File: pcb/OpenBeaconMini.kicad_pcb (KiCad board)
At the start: 2 copper layers, 100 x 80 mm, 122 parts, among them J1 Bias V, J10 BNC, J2 PAI+, J3 PAI-, J4 Digital IO, J5 SMA, J6 SMA, J7 I2C Bus, J8 ADC Inputs, J9 GND, M1 LPFModule, Q1 2N7002, Q2 MMBT4403, Q3 RD00HVS1, Q4 2N7002, Q5 2N7002, U1 TLV61046A, U2 ASTX-H11-25.000MHZ-T, U3 SN74LVC1G17, U4 SI5351A, U5 MCP4725A1T-E/CH, U6 128x32OLED, U7 Empyrean

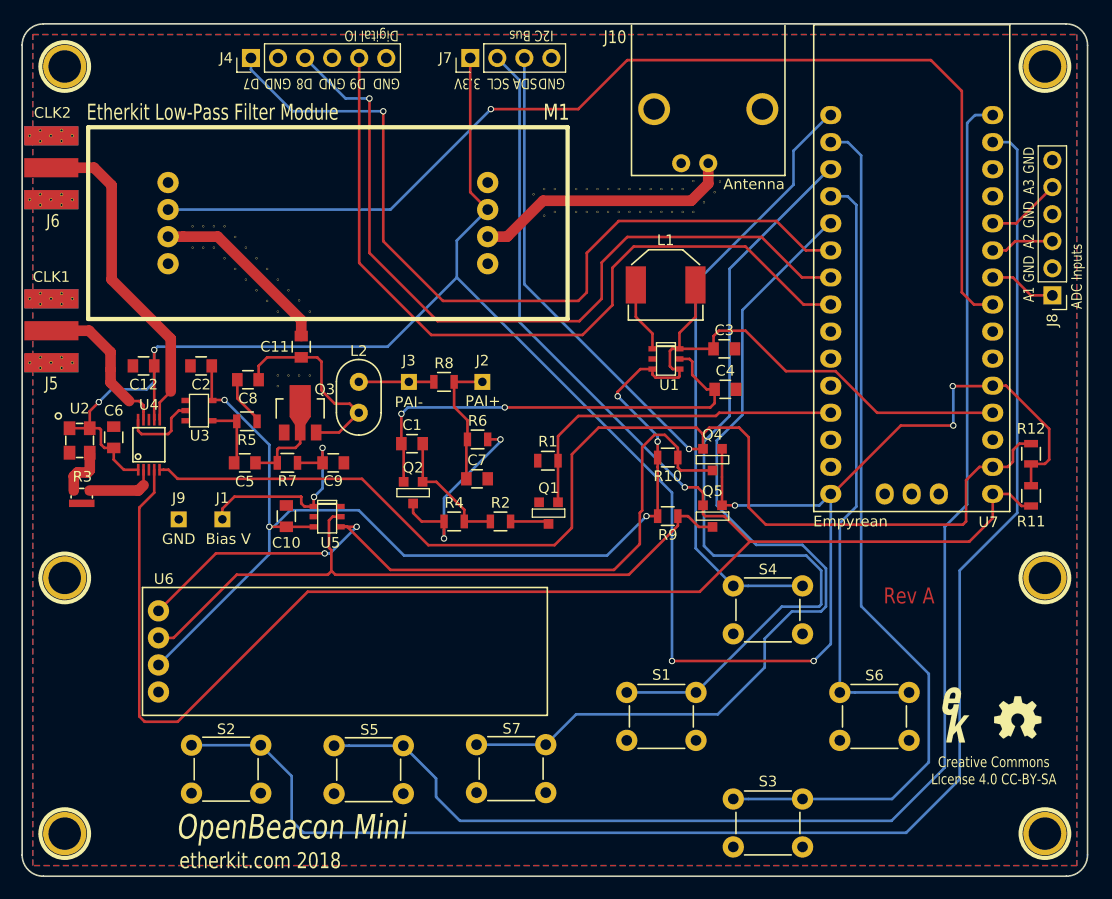
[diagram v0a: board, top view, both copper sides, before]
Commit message: Initial sl support for FT8
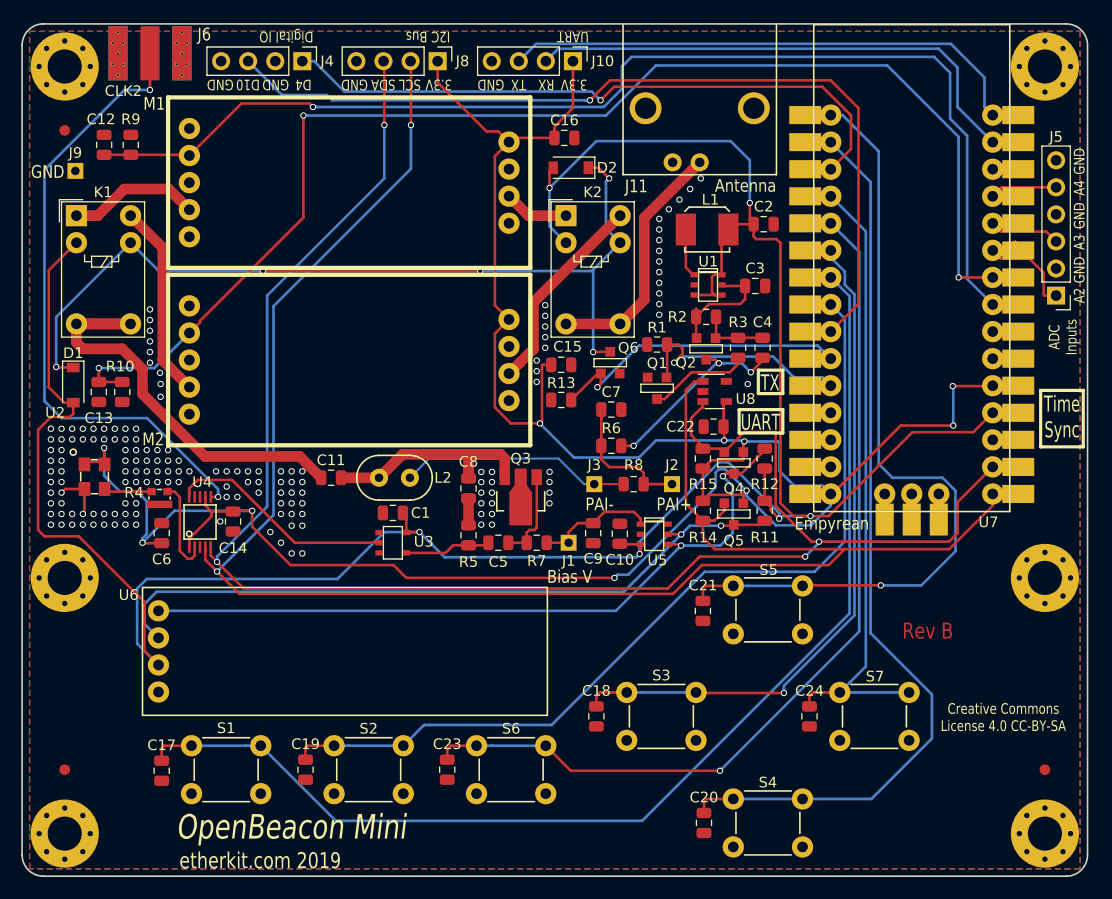
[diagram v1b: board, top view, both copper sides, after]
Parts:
- removed 1PIN (x6): P***, EtherkitKicadLibrary:MOUNTINGHOLE-4MM
- removed G***: LOGO, EtherkitKicadLibrary:OSHWLogo4mm
- removed J7: I2C Bus, Pin_Headers:Pin_Header_Straight_1x04_Pitch2.54mm
- removed Ref**: Val**, EtherkitKicadLibrary:EtherkitLogoSmall
- removed VIA (x58): VAL**, EtherkitKicadLibrary:VIA
- added C13: 100n, Capacitor_SMD:C_0805_2012Metric, F.Cu at (107.2, 84.5)
- added C14: 100n, Capacitor_SMD:C_0805_2012Metric, F.Cu at (119.8, 96.7)
- added C15: 4.7u, Capacitor_SMD:C_0805_2012Metric, F.Cu at (150.6, 82.0)
- added C16: 4.7u, Capacitor_SMD:C_0805_2012Metric, F.Cu at (150.9, 60.7)
- added C17: 100n, Capacitor_SMD:C_0805_2012Metric, F.Cu at (113.1, 120.1)
- added C18: 100n, Capacitor_SMD:C_0805_2012Metric, F.Cu at (153.9, 115.0)
- added C19: 100n, Capacitor_SMD:C_0805_2012Metric, F.Cu at (126.6, 120.0)
- added C20: 100n, Capacitor_SMD:C_0805_2012Metric, F.Cu at (164.0, 125.0)
- added C21: 100n, Capacitor_SMD:C_0805_2012Metric, F.Cu at (163.9, 105.1)
- added C22: 100n, Capacitor_SMD:C_0805_2012Metric, F.Cu at (164.9, 87.8)
- added C23: 100n, Capacitor_SMD:C_0805_2012Metric, F.Cu at (139.9, 120.0)
- added C24: 100n, Capacitor_SMD:C_0805_2012Metric, F.Cu at (173.9, 115.0)
- added D1: 1N4148W, Diode_SMD:D_SOD-123, F.Cu at (104.8, 83.9)
- added D2: 1N4148W, Diode_SMD:D_SOD-123, F.Cu at (151.5, 63.5)
- added J11: BNC, EtherkitKicadLibrary:BNC-AMPHENOL-31-5431-10RFX, F.Cu at (163.6, 50.0)
- added K1: G5V-1-DC5, Relay_THT:Relay_SPDT_Omron_G5V-1, F.Cu at (105.1, 68.0)
- added K2: G5V-1-DC5, Relay_THT:Relay_SPDT_Omron_G5V-1, F.Cu at (151.1, 68.0)
- added M2: LPF 2, EtherkitKicadLibrary:LPFModule, F.Cu at (130.7, 81.5)
- added Q6: 2N7002, EtherkitKicadLibrary:SOT23-2N7002, F.Cu at (155.2, 81.8)
- added R13: 22k, Resistor_SMD:R_0805_2012Metric, F.Cu at (150.6, 85.3)
- added R14: 3.3k, Resistor_SMD:R_0805_2012Metric, F.Cu at (163.9, 95.7)
- added R15: 3.3k, Resistor_SMD:R_0805_2012Metric, F.Cu at (163.9, 90.8)
- added REF**: Fiducial_1mm_Dia_2.54mm_Outer_CopperTop, Fiducial:Fiducial_1mm_Dia_2.54mm_Outer_CopperTop, F.Cu at (104.0, 60.0)
- added REF**: Fiducial_1mm_Dia_2.54mm_Outer_CopperTop, Fiducial:Fiducial_1mm_Dia_2.54mm_Outer_CopperTop, F.Cu at (196.0, 120.0)
- added REF**: MountingHole_3.2mm_M3_Pad_Via, MountingHole:MountingHole_3.2mm_M3_Pad_Via, F.Cu at (196.0, 102.0)
- added REF**: MountingHole_3.2mm_M3_Pad_Via, MountingHole:MountingHole_3.2mm_M3_Pad_Via, F.Cu at (104.0, 102.0)
- added REF**: MountingHole_3.2mm_M3_Pad_Via, MountingHole:MountingHole_3.2mm_M3_Pad_Via, F.Cu at (104.0, 54.0)
- added REF**: MountingHole_3.2mm_M3_Pad_Via, MountingHole:MountingHole_3.2mm_M3_Pad_Via, F.Cu at (196.0, 54.0)
- added REF**: MountingHole_3.2mm_M3_Pad_Via, MountingHole:MountingHole_3.2mm_M3_Pad_Via, F.Cu at (196.0, 126.0)
- added REF**: MountingHole_3.2mm_M3_Pad_Via, MountingHole:MountingHole_3.2mm_M3_Pad_Via, F.Cu at (104.0, 126.0)
- added REF**: Fiducial_1mm_Dia_2.54mm_Outer_CopperTop, Fiducial:Fiducial_1mm_Dia_2.54mm_Outer_CopperTop, F.Cu at (104.0, 120.0)
- added U8: 24AA64T, Package_TO_SOT_SMD:SOT-23-5, F.Cu at (165.0, 84.5)
- C1: value 10n -> 100n; footprint EtherkitKicadLibrary:C_0805 -> Capacitor_SMD:C_0805_2012Metric
- C10, C11, C12, C5, C6, C7, C8, C9: footprint EtherkitKicadLibrary:C_0805 -> Capacitor_SMD:C_0805_2012Metric
- C2: value 100n -> 2.2u; footprint EtherkitKicadLibrary:C_0805 -> Capacitor_SMD:C_0805_2012Metric
- C3: value 2.2u -> 10u; footprint EtherkitKicadLibrary:C_0805 -> Capacitor_SMD:C_0805_2012Metric
- C4: value 10u -> 10n; footprint EtherkitKicadLibrary:C_0805 -> Capacitor_SMD:C_0805_2012Metric
- J10: value BNC -> UART; footprint EtherkitKicadLibrary:BNC-AMPHENOL-31-5431-10RFX -> Connector_PinHeader_2.54mm:PinHeader_1x04_P2.54mm_Vertical
- J4: footprint Pin_Headers:Pin_Header_Straight_1x06_Pitch2.54mm -> Connector_PinHeader_2.54mm:PinHeader_1x04_P2.54mm_Vertical
- J5: value SMA -> ADC Inputs; footprint EtherkitKicadLibrary:SMA-ENDLAUNCH -> Connector_PinHeader_2.54mm:PinHeader_1x06_P2.54mm_Vertical
- J8: value ADC Inputs -> I2C Bus; footprint Pin_Headers:Pin_Header_Straight_1x06_Pitch2.54mm -> Connector_PinHeader_2.54mm:PinHeader_1x04_P2.54mm_Vertical
- M1: value LPFModule -> LPF 1
- Q3: value RD00HVS1 -> 2SK3074
- R1, R2, R5, R6, R7, R8: footprint EtherkitKicadLibrary:R_0805 -> Resistor_SMD:R_0805_2012Metric
- R10, R9: value 10k -> 270k; footprint EtherkitKicadLibrary:R_0805 -> Resistor_SMD:R_0805_2012Metric
- R11, R12: value 10k -> 3.3k; footprint EtherkitKicadLibrary:R_0805 -> Resistor_SMD:R_0805_2012Metric
- R3: value PAT1220-C-10dB -> 22k; footprint EtherkitKicadLibrary:PAT1220 -> Resistor_SMD:R_0805_2012Metric
- R4: value 22k -> PAT1220-C-10dB; footprint EtherkitKicadLibrary:R_0805 -> EtherkitKicadLibrary:PAT1220
- S1: value Left -> Menu 1
- S2: value Menu 1 -> Menu 2
- S3: value Down -> Left
- S4: value Up -> Down
- S5: value Menu 2 -> Up
- S6: value Right -> Back
- S7: value Back -> Right
- U6: value 128x32OLED -> 128x32 OLED
- moved J5 96.9 mm to (197.1, 75.5), turned to 180 degrees
- moved R3 63.2 mm to (167.2, 80.4), turned to 270 degrees
- moved J8 61.7 mm to (139.0, 53.5), turned to 270 degrees
- moved R9 61.3 mm to (110.2, 61.4), turned to 90 degrees
- moved C2 54.4 mm to (169.6, 68.8), turned to 0 degrees
- moved R10 51.6 mm to (109.4, 84.5), turned to 270 degrees
- moved S1 41.2 mm to (119.2, 120.0)
- moved S5 40.4 mm to (170.0, 105.0)
- moved S6 34.5 mm to (145.9, 120.0)
- moved S7 34.5 mm to (180.0, 115.0)
- moved J9 34.1 mm to (105.0, 63.8)
- moved J1 32.6 mm to (151.3, 98.7)
- moved C10 31.3 mm to (156.1, 97.8)
- moved U5 30.7 mm to (159.3, 97.9)
- moved Q2 30.6 mm to (164.2, 80.5)
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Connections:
- net A5 renamed Net-(U7-Pad13)
- C1 pad 1: Net-(C1-Pad1) -> +5V
- C1 pad 2: Net-(C1-Pad2) -> GND
- C12 pad 1: +3.3V -> BAND_ID_1
- C3 pad 1: +5V -> Net-(C3-Pad1)
- C4 pad 1: Net-(C1-Pad1) -> Net-(C4-Pad1)
- C4 pad 2: GND -> Net-(C4-Pad2)
- J10 pad 1: Net-(J10-Pad1) -> +3.3V
- J10 pad 2: GND -> UART_RX
- J4 pad 1: D7 -> D4
- J4 pad 3: D8 -> D10
- J5 pad 1: Net-(J5-Pad1) -> A2
- J8 pad 1: A1 -> +3.3V
- J8 pad 2: GND -> SCL
- J8 pad 3: A2 -> SDA
- M1 pad 2: BAND_ID -> BAND_ID_1
- M1 pad 3: Net-(C11-Pad1) -> GND
- M1 pad 4: GND -> Net-(K1-Pad1)
- M1 pad 6: Net-(J10-Pad1) -> GND
- M1 pad 7: +3.3V -> Net-(K2-Pad1)
- Q2 pad 1: Net-(C1-Pad1) -> Net-(C3-Pad1)
- Q2 pad 2: Net-(C1-Pad2) -> Net-(C4-Pad2)
- Q2 pad 3: Net-(Q2-Pad3) -> Net-(C4-Pad1)
- R10 pad 1: +5V -> BAND_ID_2
- R10 pad 2: SDA_5V -> GND
- R11 pad 1: +3.3V -> +5V
- R11 pad 2: SCL -> SCL_5V
- R12 pad 1: +3.3V -> +5V
- R12 pad 2: SDA -> SDA_5V
- R2 pad 1: Net-(C1-Pad2) -> Net-(C3-Pad1)
- R2 pad 2: Net-(Q1-Pad3) -> Net-(C4-Pad2)
- R3 pad 1: Net-(R3-Pad1) -> Net-(C4-Pad2)
- R3 pad 2: Net-(R3-Pad2) -> Net-(Q1-Pad3)
- R4 pad 1: Net-(Q2-Pad3) -> Net-(R4-Pad1)
- R4 pad 2: Net-(C1-Pad2) -> Net-(R4-Pad2)
- R6 pad 2: Net-(Q2-Pad3) -> Net-(C4-Pad1)
- R9 pad 1: +5V -> BAND_ID_1
- R9 pad 2: SCL_5V -> GND
- S1 pad 1: BTN_LEFT -> BTN_DSP_1
- S1 pad 2: BTN_LEFT -> BTN_DSP_1
- S2 pad 1: BTN_DSP_1 -> GND
- S2 pad 2: BTN_DSP_1 -> GND
- S2 pad 3: GND -> BTN_DSP_2
- S2 pad 4: GND -> BTN_DSP_2
- S3 pad 1: GND -> BTN_LEFT
- S3 pad 2: GND -> BTN_LEFT
- S3 pad 3: BTN_DOWN -> GND
- S3 pad 4: BTN_DOWN -> GND
- S4 pad 3: BTN_UP -> BTN_DOWN
- S4 pad 4: BTN_UP -> BTN_DOWN
- S5 pad 3: BTN_DSP_2 -> BTN_UP
- S5 pad 4: BTN_DSP_2 -> BTN_UP
- S6 pad 3: BTN_RIGHT -> BTN_BACK
- S6 pad 4: BTN_RIGHT -> BTN_BACK
- S7 pad 3: BTN_BACK -> BTN_RIGHT
- S7 pad 4: BTN_BACK -> BTN_RIGHT
- U1 pad 5: Net-(C1-Pad1) -> Net-(C3-Pad1)
- U2 pad 3: Net-(R3-Pad1) -> Net-(R4-Pad1)
- U4 pad 2: Net-(R3-Pad2) -> Net-(R4-Pad2)
- U4 pad 9: Net-(J5-Pad1) -> Net-(U4-Pad9)
- U7 pad 14: BTN_DSP_1 -> UART_RX
- U7 pad 15: BTN_DSP_2 -> UART_TX
- U7 pad 18: BTN_LEFT -> D4
- U7 pad 21: D7 -> BTN_LEFT
- U7 pad 22: D8 -> BTN_DSP_1
- U7 pad 23: D9 -> BTN_DSP_2
- U7 pad 25: D11 -> BAND_SW
- U7 pad 26: Net-(U7-Pad26) -> TX
- U7 pad 27: TX -> Net-(U7-Pad27)
- U7 pad 8: BAND_ID -> BAND_ID_1
- U7 pad 9: A1 -> BAND_ID_2
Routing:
- net BAND_ID_2: track 0.00 -> 122.7 mm, vias 0 -> 3
- net BAND_ID_1: track 0.00 -> 108.8 mm, vias 0 -> 1
- net BAND_ID: track 103.8 -> 0.00 mm, vias 1 -> 0
- net +5V: track 145.2 -> 245.2 mm, vias 5 -> 6
- net BAND_RELAY: track 0.00 -> 82.7 mm, vias 0 -> 5
- net D10: track 0.00 -> 82.7 mm, vias 0 -> 1
- net D7: track 78.1 -> 0.00 mm, vias 1 -> 0
- net D8: track 74.9 -> 0.00 mm, vias 1 -> 0
- net D9: track 74.0 -> 0.00 mm
- net D4: track 0.00 -> 60.6 mm, vias 0 -> 1
- net UART_RX: track 0.00 -> 50.8 mm
- net UART_TX: track 0.00 -> 49.5 mm
- net BTN_DSP_2: track 127.4 -> 82.6 mm
- net Net-(C1-Pad1): track 42.8 -> 0.00 mm, vias 2 -> 0
- net BTN_DSP_1: track 144.0 -> 109.1 mm
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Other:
- board text added: "A4"
- board text added: "D10"
- board text added: "D4"
- board text added: "RX"
- board text added: "Rev B"
- board text added: "TX"
- board text added: "Time Sync"
- board text added: "UART"
- board text added: "etherkit.com 2019"
- board text removed: "A1"
- board text removed: "CLK1"
- board text removed: "D7"
- board text removed: "D8"
- board text removed: "D9"
- board text removed: "Etherkit Low-Pass Filter Module"
- board text removed: "Rev A"
- board text removed: "etherkit.com 2018"
